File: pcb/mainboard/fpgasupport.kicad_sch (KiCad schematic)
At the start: 35 parts

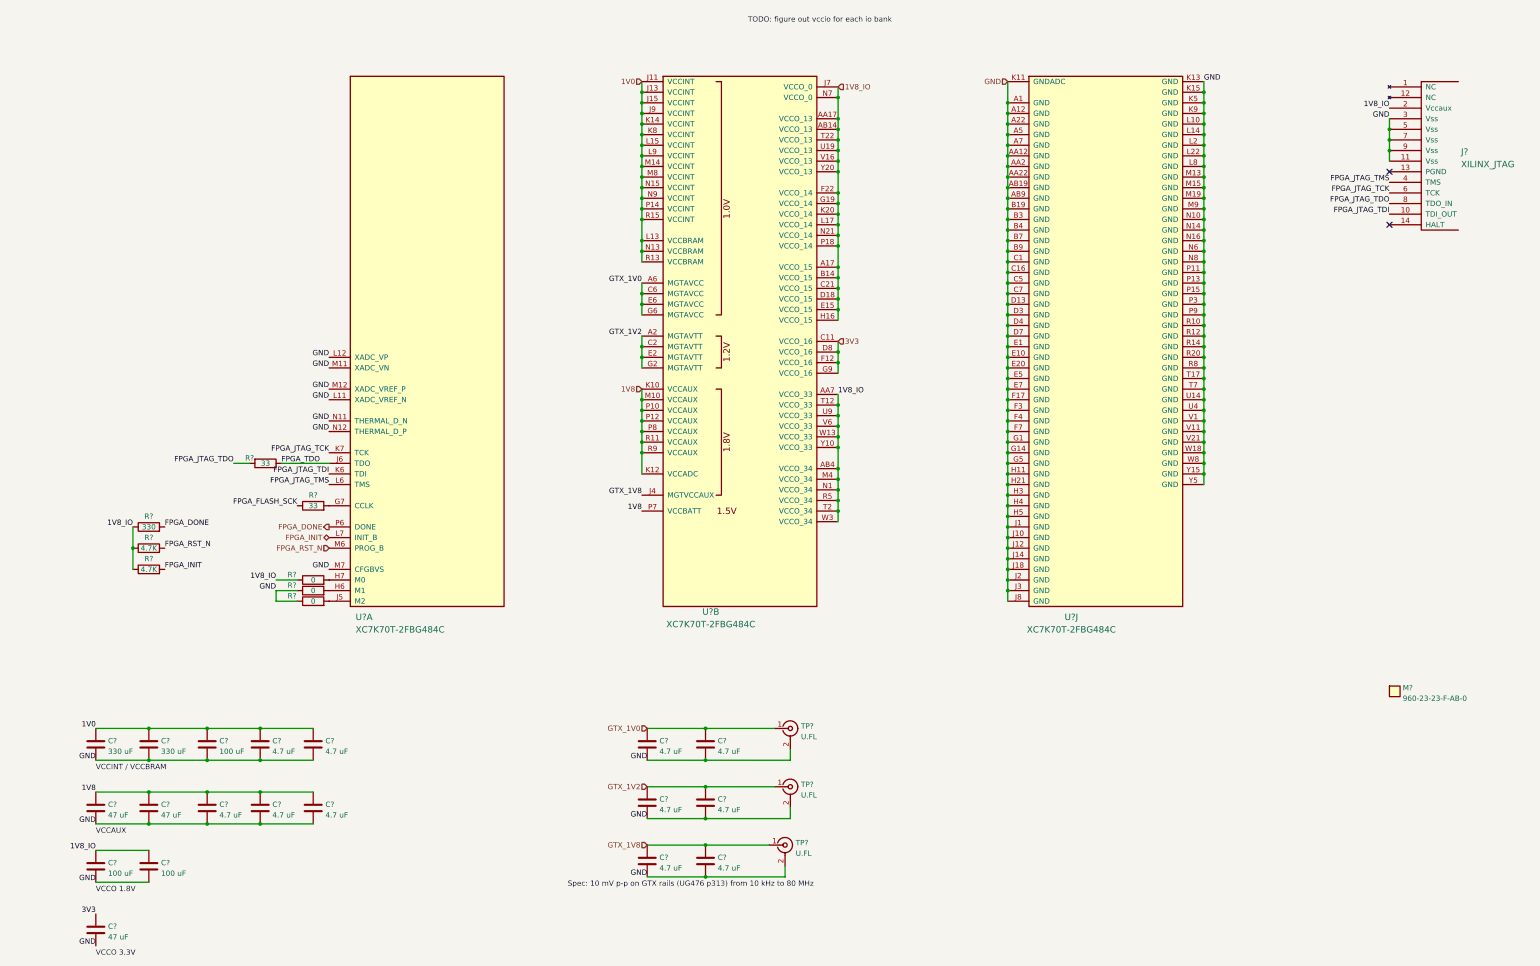
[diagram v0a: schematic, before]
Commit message: Continued initial work on main board
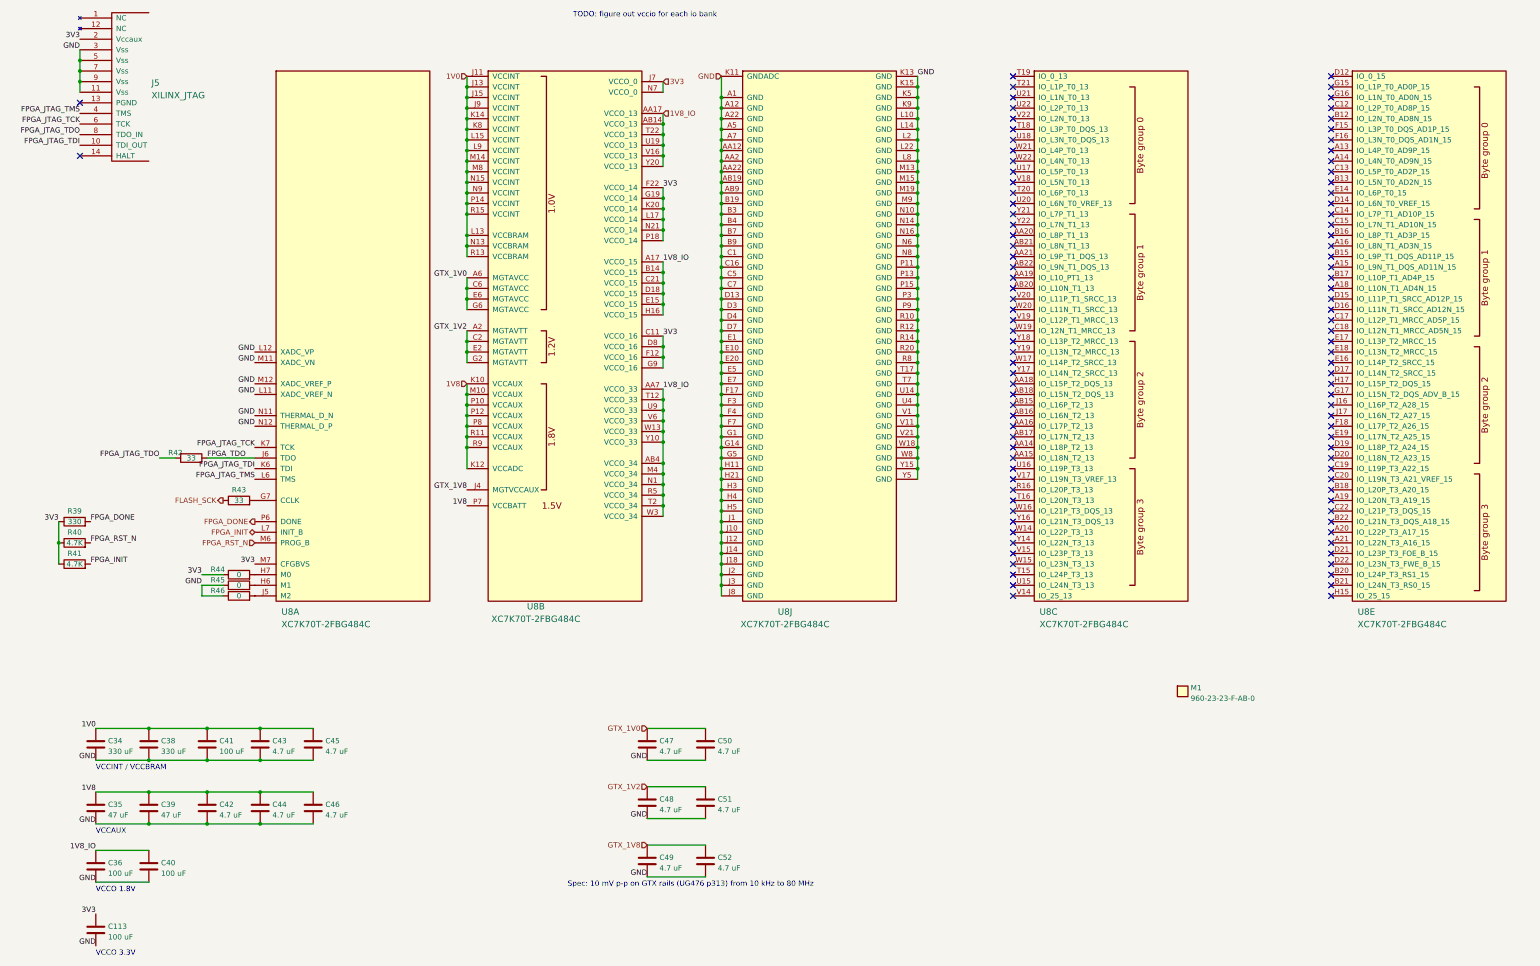
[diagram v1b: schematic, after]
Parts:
- removed C?: 47 uF, azonenberg_pcb:EIA_1210_CAP_NOSILK, symbol device:C
- removed TP? (x3): U.FL, azonenberg_pcb:CONN_U.FL_TE_1909763-1, symbol conn:CONN_COAXIAL
- added C113: 100 uF, symbol device:C
- added unit 5 of U8
- added unit 3 of U8
- C34, C35, C38, C39: renamed from C?; footprint azonenberg_pcb:EIA_1210_CAP_NOSILK -> (none)
- C36, C40, C41: renamed from C?; footprint azonenberg_pcb:EIA_1206_CAP_NOSILK -> (none)
- C42, C43, C44, C45, C46, C47, C48, C49, C50, C51, C52: renamed from C?; footprint azonenberg_pcb:EIA_0603_CAP_NOSILK -> (none)
- J5: renamed from J?; footprint azonenberg_pcb:XILINX_JTAG_PTH_MOLEX_0878311420 -> (none)
- M1: renamed from M?; footprint azonenberg_pcb:HEATSINK_WAKEFIELDVETTE_960-23-23-F-AB-0 -> (none)
- R39, R40, R41, R42, R43, R44, R45, R46: renamed from R?; footprint azonenberg_pcb:EIA_0402_RES_NOSILK -> (none)
- U8: renamed from U?; footprint azonenberg_pcb:BGA_484_22x22_FULLARRAY_1MM -> (none)
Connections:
- net 1V8_IO: no longer J5.2 (Vccaux), R39.1, R40.1, R41.1, R44.1, U8.F22 (VCCO_14), U8.G19 (VCCO_14), U8.J7 (VCCO_0), U8.K20 (VCCO_14), U8.L17 (VCCO_14), U8.N21 (VCCO_14), U8.N7 (VCCO_0), U8.P18 (VCCO_14)
- net 3V3: now also J5.2 (Vccaux), R39.1, R40.1, R41.1, R44.1, U8.F22 (VCCO_14), U8.G19 (VCCO_14), U8.J7 (VCCO_0), U8.K20 (VCCO_14), U8.L17 (VCCO_14), U8.M7 (CFGBVS), U8.N21 (VCCO_14), U8.N7 (VCCO_0), U8.P18 (VCCO_14), C113.1
- net GND: now also C113.2; no longer U8.M7 (CFGBVS)
- net FPGA_FLASH_SCK renamed FLASH_SCK
- no-connect marks 2 -> 102
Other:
- moved on the sheet: J5, M1, R39, R40, R41, R42, R43, R44, R45, R46, U8A, U8B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

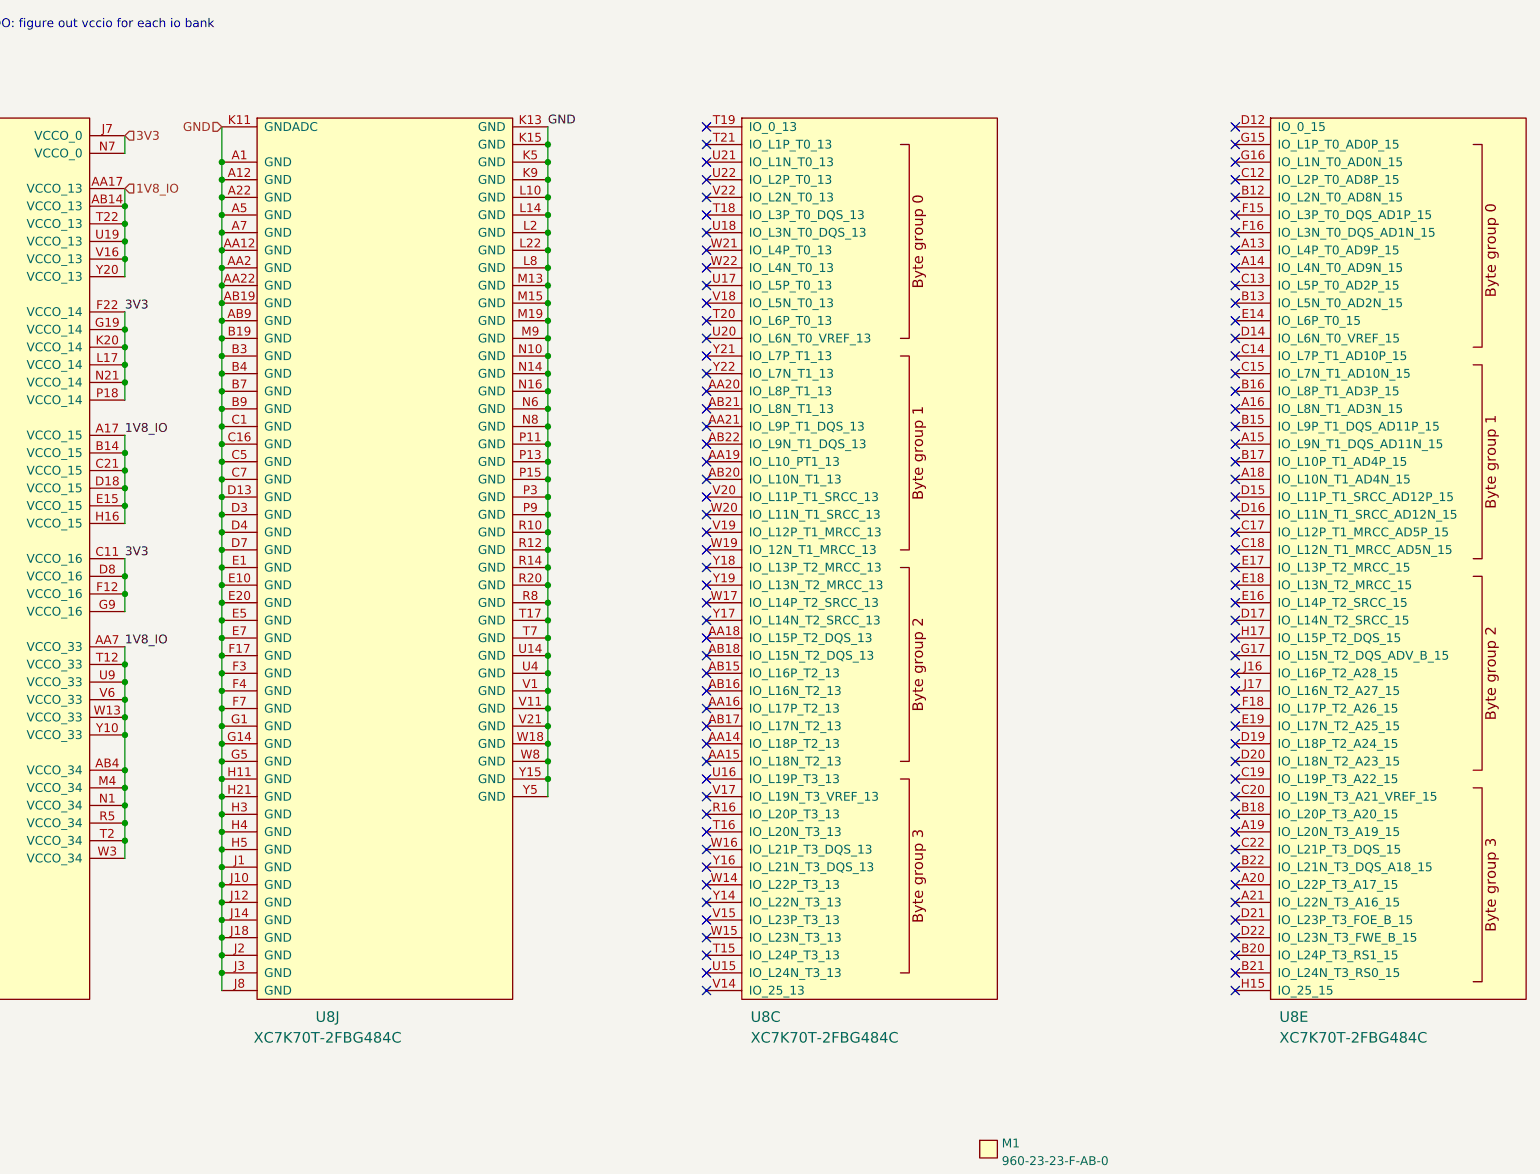
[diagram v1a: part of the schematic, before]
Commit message: Finished initial iteration of schematic, needs a verification pass to check for missing features then schematic review
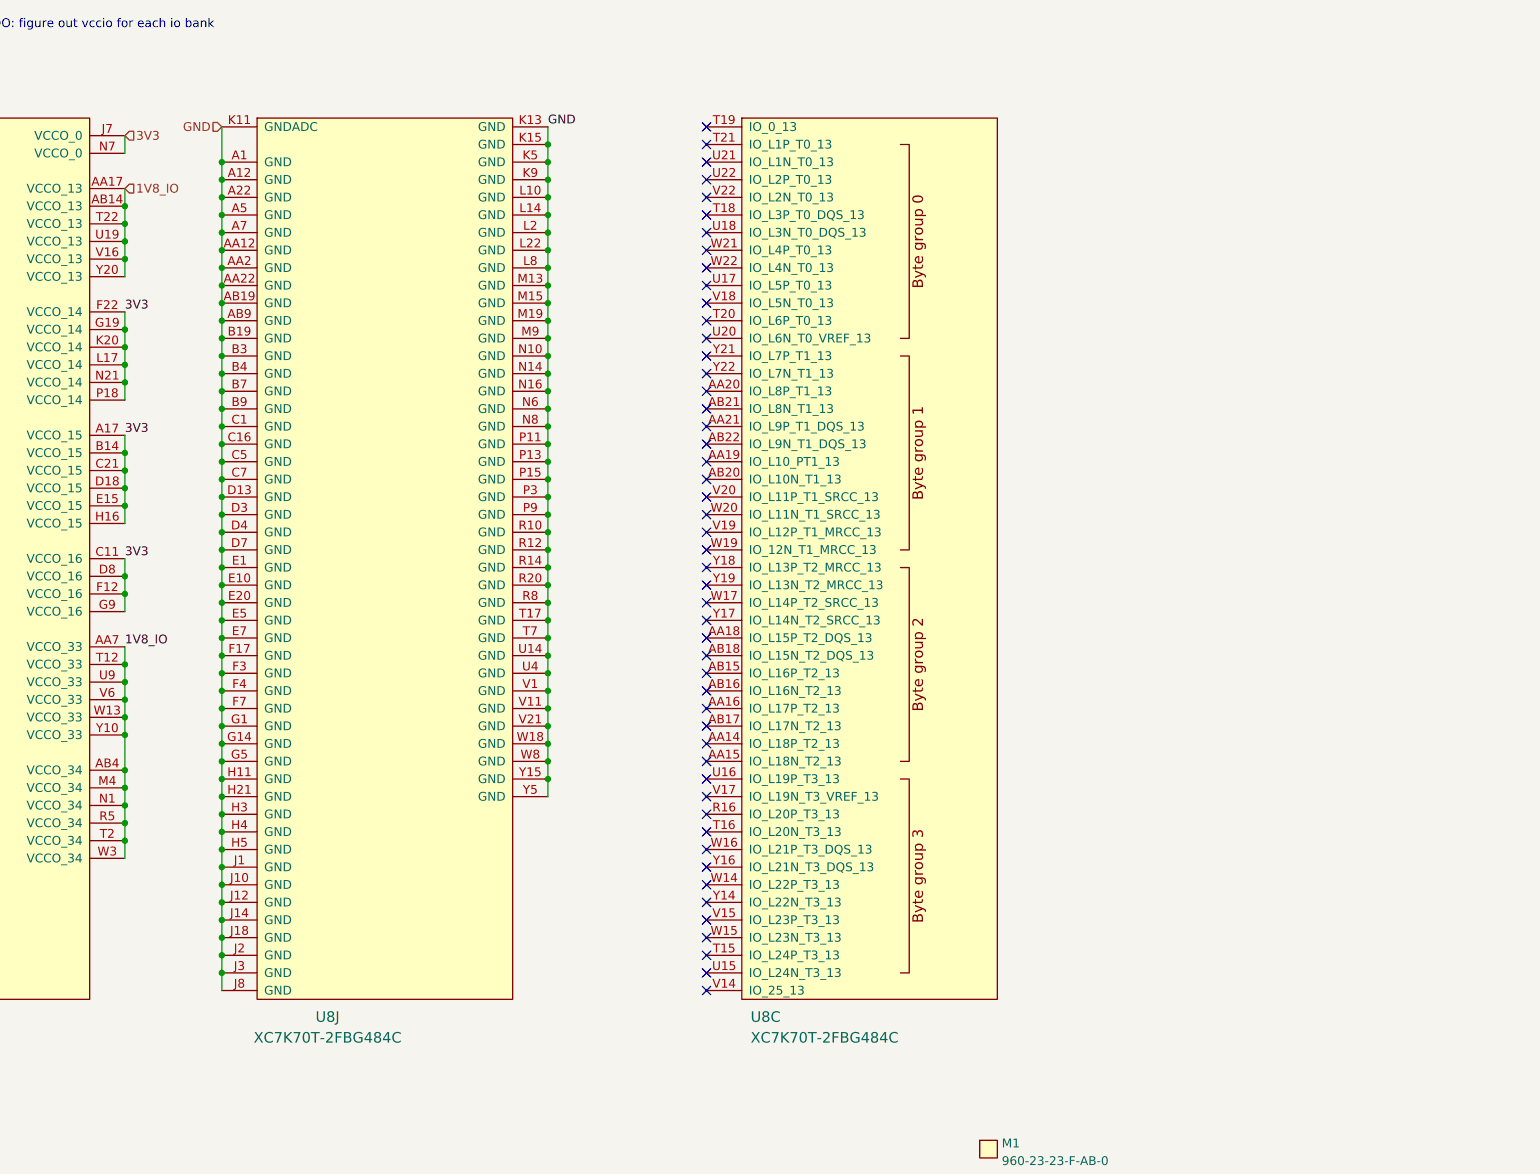
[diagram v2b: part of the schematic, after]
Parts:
- removed unit 5 of U8
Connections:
- net 1V8_IO: no longer U8.A17 (VCCO_15), U8.B14 (VCCO_15), U8.C21 (VCCO_15), U8.D18 (VCCO_15), U8.E15 (VCCO_15), U8.H16 (VCCO_15)
- net 3V3: now also U8.A17 (VCCO_15), U8.B14 (VCCO_15), U8.C21 (VCCO_15), U8.D18 (VCCO_15), U8.E15 (VCCO_15), U8.H16 (VCCO_15)
- no-connect marks 102 -> 52

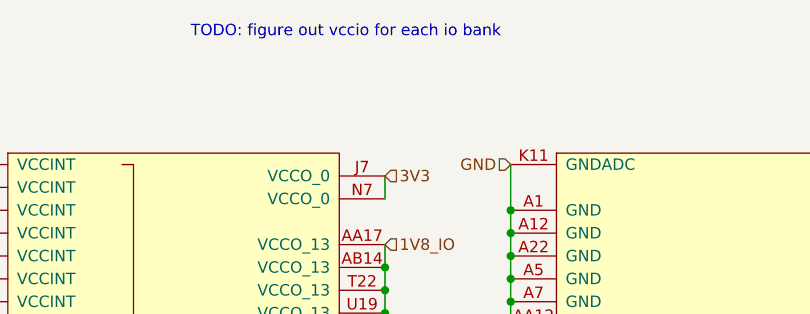
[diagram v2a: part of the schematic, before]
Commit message: Added missing decoupling caps to comparator
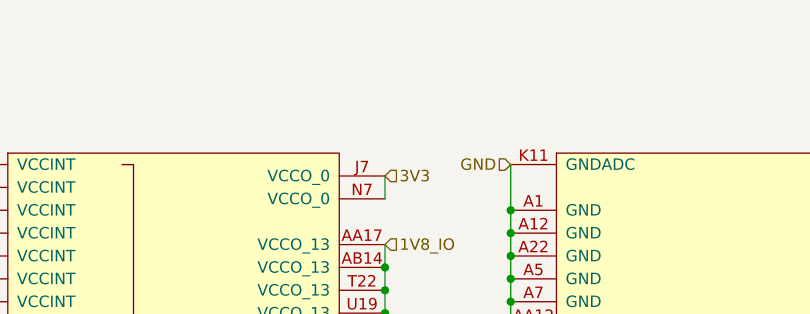
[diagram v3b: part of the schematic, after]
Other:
- note removed: "TODO: figure out vccio for each io bank"
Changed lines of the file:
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@@
-    (effects (font (size 1.27 1.27)) (justify left bottom))
-  )
-  (text "TODO: figure out vccio for each io bank" (at 153.67 27.94 0)
     (effects (font (size 1.27 1.27)) (justify left bottom))
   )

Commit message: Calculated power monitor voltage divider
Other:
- company: (none) -> Antikernel Labs
- title: (none) -> Trigger Crossbar
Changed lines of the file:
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@@
 (kicad_sch (version 20211123) (generator eeschema)
   (paper "A3")
+  (title_block
+    (title "Trigger Crossbar")
+    (date "2023-12-17")
+    (rev "0.1")
+    (company "Antikernel Labs")
+    (comment 1 "Andrew D. Zonenberg")
+  )
   (junction (at 175.26 78.74) (diameter 0) (color 0 0 0 0)
   )
